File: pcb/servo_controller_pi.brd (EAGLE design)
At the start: 71 parts, among them IC1 PIC18F452, IC3 MAX4173FESA+, IC4 LM2936MP-3.3, IC5 4512D, IC6 LM386M-1, Q1 10Mhz, Q4 BC848ALT1SMD

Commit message: BleuettePi
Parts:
- removed LED2: (no value), led:CHIPLED_0805
- removed SJ1: (no value), jumper:SJ
- removed U$1: (no value), ohw-logo:OSHW_8X100_NOTEXT
- added C8: (no value), rcl:PANASONIC_A
- added HP+, HP-: (no value), wirepad:2,54/0,8
- added PWR: (no value), led:CHIPLED_0805
- added U$5: (no value), ohw-logo:OSHW_6X150_NOTEXT
- moved C17 12.9 mm to (78.4, 21.3)
- moved U$2 12.0 mm to (41.0, 18.4), turned to 0 degrees
- moved R15 8.98 mm to (70.5, 14.0), turned to 180 degrees
- moved C15 8.76 mm to (76.5, 14.0)
- moved R3 8.26 mm to (74.9, 21.3), turned to 180 degrees
- moved R12 7.63 mm to (25.7, 14.3)
- moved IC6 6.38 mm to (70.5, 20.3)
- moved C14 6.24 mm to (76.5, 17.8)
- moved SV4 4.49 mm to (81.3, 14.6)
- moved R2 4.24 mm to (13.7, 25.4)
- moved D3 4.14 mm to (10.2, 26.4)
- moved R9 4.13 mm to (25.4, 18.3)
- moved D6 3.82 mm to (27.9, 20.3)
- moved R1 3.62 mm to (7.30, 25.4), turned to 270 degrees
- moved R10 3.49 mm to (30.5, 18.3)
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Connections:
- new net N$9: C16.-, HP+.1
- net +3V3: now also PWR.C; no longer LED2.C
- net +5V: now also C8.+
- net N$39: now also PWR.A; no longer LED2.A
- net VSS: now also C8.-, HP-.1
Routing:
- net +5V: track 92.4 -> 245.8 mm, vias 1 -> 4
- net DI: track 0.00 -> 85.7 mm
- net SI: track 0.00 -> 77.2 mm
- net TX_PI: track 0.00 -> 49.3 mm, vias 0 -> 3
- net RX_PI: track 3.83 -> 46.7 mm, vias 0 -> 1
- net SDA: track 46.5 -> 78.0 mm
- net N$21: track 0.00 -> 10.4 mm
- net N$34: track 15.6 -> 24.7 mm
- net VSS: track 87.0 -> 93.8 mm, vias 10 -> 13
- net N$7: track 0.00 -> 6.76 mm
- net N$41: track 0.00 -> 6.01 mm
- net N$23: track 23.6 -> 17.7 mm
- net N$42: track 0.00 -> 5.93 mm
- net N$18: track 11.3 -> 16.8 mm
- net OPTION2: track 20.3 -> 14.8 mm
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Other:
- board text added: "BleuettePi"
- board text added: "Rev. 1.0.0"
- board text removed: "ON"
- board text removed: "Rev. 1.2.1"

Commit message: BleuettePi
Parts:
- added T3.3V, T5V, T6V: TPB1,27, testpad:B1,27
- added TP1: TPSQPAD1-13, testpad:P1-13
- moved U$2 2.62 mm to (41.6, 15.9)
- moved C12 1.85 mm to (66.7, 23.2), turned to 270 degrees
- moved R13 0.64 mm to (70.5, 33.0)
- renumbered SV5 to OPTION
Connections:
- net +3V3: now also T3.3V.TP
- net +5V: now also T5V.TP
- net VEE: now also T6V.TP
- net VSS: now also TP1.TP
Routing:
- net +5V: track 245.8 -> 243.8 mm
- net VEE: track 179.9 -> 181.5 mm
- net OUT: track 76.8 -> 75.5 mm
- net +3V3: track 176.1 -> 177.1 mm
- net N$37: track 5.75 -> 6.38 mm
- net SCL: track 74.8 -> 75.4 mm
- net VSS: vias 13 -> 10
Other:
- board text added: "3.3V"
- board text added: "5V"
- board text added: "6V"
- board text added: "GND"
- board text added: "HP"
- board text added: "L"
- board text added: "LED Strip"
- board text added: "R"
- board text removed: "-"
- board text removed: "Bleuette"

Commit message: BleuettePi
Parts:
- removed T3.3V, T5V, T6V: TPB1,27, testpad:B1,27
- added AN6, T_3.3V, T_5V, T_6V, T_LVOLTAGE, T_RX_PI, T_TX_PI: TPB1,27, testpad:B1,27
- added T_CURRENT: TPSQPAD1-13, testpad:P1-13
- HP+, HP-, P5V, PGND, PLIPO: device wirepad:2,54/0,8 -> wirepad:2,15/1,0
- moved U$5 60.7 mm to (26.4, 33.0)
- moved HP- 1.90 mm to (81.3, 23.2)
- moved P5V 1.27 mm to (3.81, 25.4)
- moved TP1 1.27 mm to (2.38, 35.9)
- moved D2 1.27 mm to (3.81, 2.54)
- moved PGND 1.27 mm to (3.81, 20.3)
- moved C16 0.32 mm to (76.2, 25.7)
- moved HP+ 0.32 mm to (81.3, 25.7)
- moved C5 0.32 mm to (2.86, 10.8)
- renumbered U$4 to IC7
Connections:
- new net N$20: IC1.27
- new net N$26: AN6.TP, IC1.26
- net +3V3: now also T_3.3V.TP; no longer T3.3V.TP
- net +5V: now also T_5V.TP; no longer T5V.TP
- net LIPO_VOLTAGE: now also T_LVOLTAGE.TP
- net RX_PI: now also T_RX_PI.TP
- net SERVO_CURRENT: now also T_CURRENT.TP
- net TX_PI: now also T_TX_PI.TP
- net VEE: now also T_6V.TP; no longer T6V.TP
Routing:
- net VSS: track 93.8 -> 107.7 mm, vias 10 -> 12
- net +5V: track 243.8 -> 241.5 mm
- net LIPO_VOLTAGE: track 46.8 -> 48.9 mm
- net N$26: track 0.00 -> 1.66 mm
- net +3V3: track 177.1 -> 175.5 mm
- net TX_PI: track 49.3 -> 50.3 mm
- net RX_PI: track 46.7 -> 47.7 mm
- net VEE: track 181.5 -> 182.3 mm
- net VDD: track 31.5 -> 32.0 mm
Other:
- board text added: "C"
- board text added: "GY-27"
- board text added: "LED STRIP"
- board text added: "RX Pi"
- board text added: "TX Pi"
- board text added: "V"
- board text removed: "LED Strip"

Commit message: RaspberryPi
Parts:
- added DRDY: (no value), jumper:SJ
- U$3: value RASPBERRY-PI -> RASPBERRY-PILIGHT-HOLE; device RaspberryPi:RASPBERRY-PI -> RaspberryPi:RASPBERRY-PI-LIGHT-HOLE
- moved U$5 60.8 mm to (79.7, 3.81)
- moved U$3 45.5 mm to (41.9, 27.9)
- moved D6 14.5 mm to (25.4, 34.6), turned to 90 degrees
- moved R9 5.91 mm to (30.5, 21.3), turned to 270 degrees
- moved SV1 3.81 mm to (73.0, 48.9)
- moved SV2 3.81 mm to (52.1, 48.9)
- moved RN1 3.18 mm to (63.5, 43.5)
- moved IC5 2.54 mm to (63.5, 36.2)
- moved C6 2.22 mm to (67.6, 30.5)
- moved R13 2.22 mm to (70.5, 35.2)
- moved C8 1.59 mm to (77.5, 32.4)
- moved R12 1.42 mm to (25.1, 13.0)
- moved T_3.3V 1.14 mm to (73.3, 30.5)
- moved R10 0.95 mm to (31.4, 18.3)
- moved R11 0.95 mm to (31.4, 16.2)
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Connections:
- new net N$36: DRDY.2, IC7.DRY
- net OPTION4: now also DRDY.1
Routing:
- net OPTION4: track 19.7 -> 66.0 mm
- net +5V: track 241.5 -> 252.8 mm, vias 4 -> 3
- net VSS: track 107.7 -> 98.8 mm, vias 12 -> 11
- net ADDRA: track 53.2 -> 49.8 mm
- net OUT: track 75.5 -> 72.4 mm
- net ADDRB: track 49.0 -> 45.9 mm
- net ADDRC: track 48.3 -> 45.2 mm
- net N$33: track 20.8 -> 23.5 mm
- net N$18: track 16.8 -> 19.5 mm
- net N$34: track 24.7 -> 27.4 mm
- net N$36: track 0.00 -> 2.59 mm
- net +3V3: track 175.5 -> 178.0 mm
- net N$28: track 13.9 -> 15.8 mm
- net RX_PI: track 47.7 -> 49.6 mm
- net N$30: track 12.8 -> 14.7 mm
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
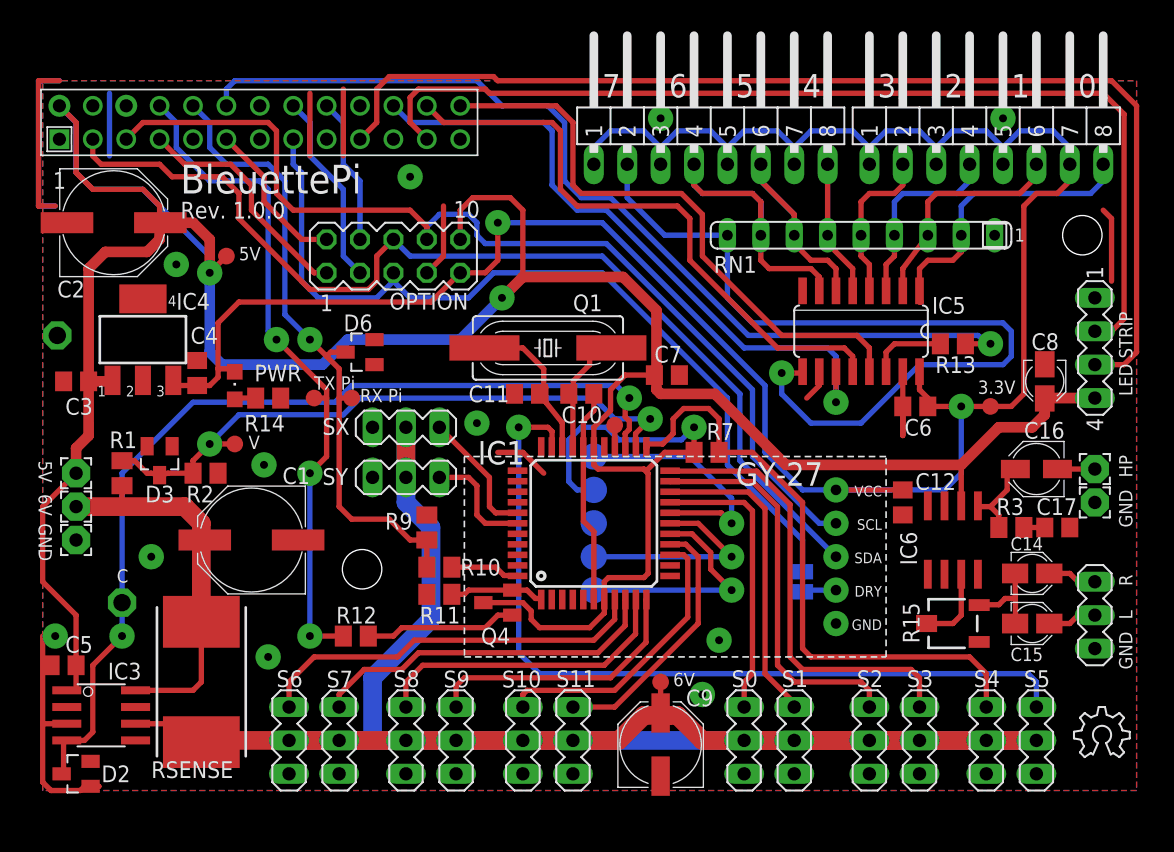
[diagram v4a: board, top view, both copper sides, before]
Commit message: Raspberry Pi PCB version
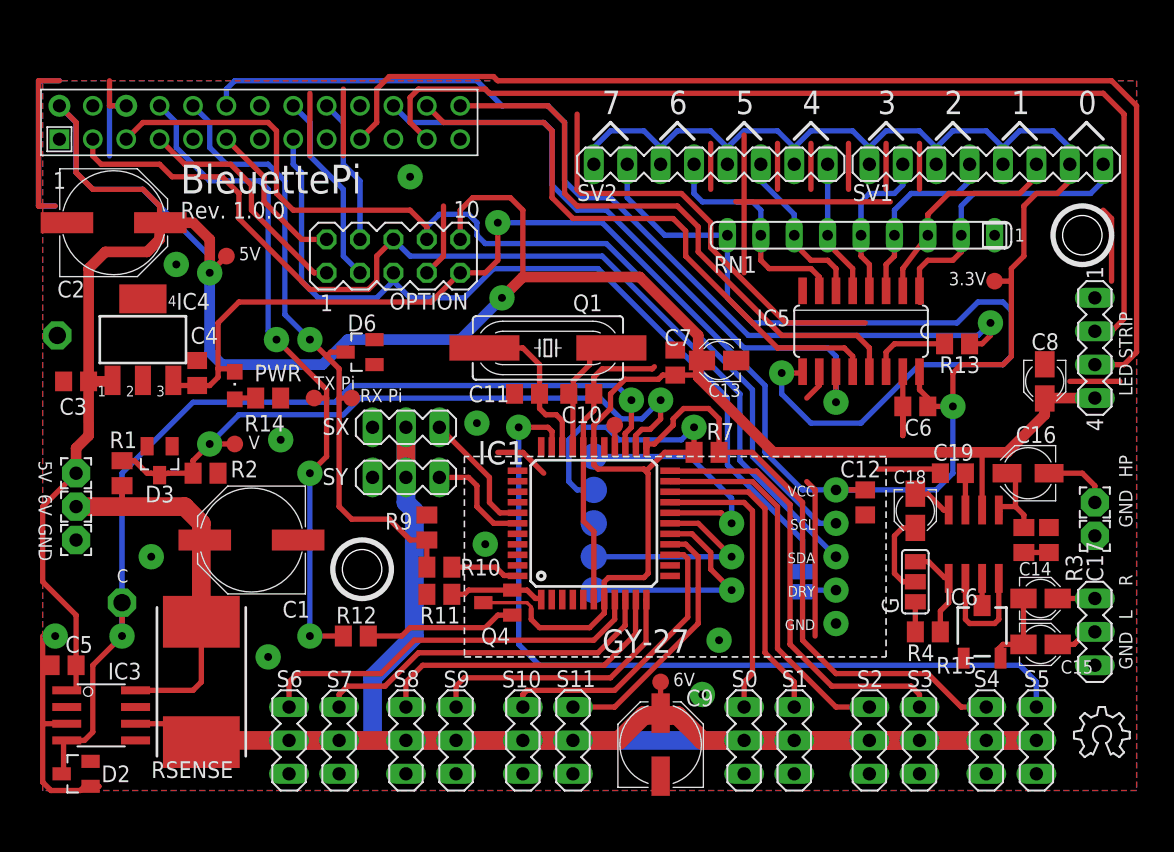
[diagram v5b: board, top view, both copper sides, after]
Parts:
- added C13: (no value), rcl:PANASONIC_A
- added C18: 10uf, rcl:PANASONIC_A
- added C19: (no value), rcl:C0805
- added G: (no value), jumper:SJ_2
- added R4: 1k, rcl:M0805
- C14, C15: value (none) -> 4.7uf
- SV1, SV2: device con-lstb:MA08-1W -> con-lstb:MA08-1
- moved T_3.3V 9.53 mm to (73.7, 40.0)
- moved C12 2.86 mm to (63.8, 23.2)
- moved HP+ 2.54 mm to (81.3, 23.2)
- moved HP- 2.54 mm to (81.3, 20.6)
- moved R15 2.31 mm to (72.7, 13.3), turned to 90 degrees
- moved C14 2.01 mm to (77.2, 15.9)
- moved C15 1.71 mm to (77.2, 12.4)
- moved IC6 1.62 mm to (72.1, 20.0)
- moved R3 1.35 mm to (75.9, 20.3), turned to 90 degrees
- moved SV4 1.27 mm to (81.3, 13.3)
- moved C17 1.14 mm to (77.8, 20.3), turned to 90 degrees
- moved C7 1.14 mm to (49.4, 33.8), turned to 90 degrees
- moved C16 0.71 mm to (76.2, 25.4)
- moved R13 0.32 mm to (70.8, 35.2)
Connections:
- new net N$38: G.3, IC6.1, R4.2
- new net N$44: G.1, R4.1
- new net N$45: C18.+, G.2
- new net N$46: C18.-, IC6.8
- new net N$47: C19.1, IC6.7
- net +5V: now also C13.+
- net VSS: now also C13.-, C19.2
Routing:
- net VSS: track 98.8 -> 215.5 mm, vias 11 -> 10
- net N$34: track 27.4 -> 17.7 mm
- net N$38: track 0.00 -> 7.40 mm
- net N$45: track 0.00 -> 6.55 mm
- net N$18: track 19.5 -> 13.1 mm
- net N$28: track 15.8 -> 10.4 mm
- net +5V: track 252.8 -> 257.8 mm
- net N$41: track 6.01 -> 2.07 mm
- net LIPO_VOLTAGE: track 48.9 -> 52.4 mm
- net N$46: track 0.00 -> 3.05 mm
- net +3V3: track 178.0 -> 175.0 mm
- net N$47: track 0.00 -> 2.80 mm
- net SERVO_CURRENT: track 71.4 -> 73.9 mm
- net N$9: track 2.84 -> 5.14 mm
- net N$44: track 0.00 -> 2.29 mm
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
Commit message: Raspberry Pi
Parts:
- added AN7, RC1, RC2, RC3, RC4, RC5, RD2, RD3, RD4, RD5, RD6, RD7: TPSQTP06SQ, testpad:TP06SQ
- added P6V: (no value), wirepad:2,15/1,0
- AN6: value TPB1,27 -> TPSQTP06SQ; device testpad:B1,27 -> testpad:TP06SQ
- moved R1 2.56 mm to (6.99, 22.9), turned to 180 degrees
- moved PGND 2.54 mm to (3.81, 17.8)
- moved T_3.3V 2.31 mm to (75.9, 39.4)
- moved DRDY 1.27 mm to (59.1, 18.4)
- moved D3 0.63 mm to (10.2, 25.7)
- moved C4 0.48 mm to (13.5, 33.0)
- moved AN6 0.32 mm to (44.8, 28.7)
- moved C18 0.32 mm to (67.6, 22.2)
- renumbered PLIPO to PBATT
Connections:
- new net +7V: C1.+, IC3.8, P6V.1, RSENSE.1
- new net N$48: IC1.5, RD7.TP
- new net N$49: IC1.4, RD6.TP
- new net N$50: IC1.3, RD5.TP
- new net N$51: IC1.2, RD4.TP
- new net N$52: IC1.36, RC2.TP
- new net N$53: IC1.35, RC1.TP
- new net N$54: IC1.37, RC3.TP
- new net N$55: IC1.42, RC4.TP
- new net N$56: IC1.43, RC5.TP
- new net N$57: IC1.41, RD3.TP
- new net N$58: IC1.40, RD2.TP
- net N$20: now also AN7.TP
- net VDD: no longer C1.+, IC3.8, RSENSE.1
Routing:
- net VDD: track 32.0 -> 2.23 mm
- net +7V: track 0.00 -> 27.6 mm
- net VSS: track 215.5 -> 224.3 mm
- net N$51: track 0.00 -> 1.37 mm
- net N$56: track 0.00 -> 1.37 mm
- net N$53: track 0.00 -> 1.37 mm
- net N$55: track 0.00 -> 1.36 mm
- net N$52: track 0.00 -> 1.36 mm
- net N$50: track 0.00 -> 1.36 mm
- net N$57: track 0.00 -> 1.36 mm
- net N$54: track 0.00 -> 1.36 mm
- net N$49: track 0.00 -> 1.36 mm
- net N$58: track 0.00 -> 1.35 mm
- net N$48: track 0.00 -> 1.35 mm
- net N$20: track 0.00 -> 1.35 mm
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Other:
- board text added: "BT"

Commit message: BleuettePi
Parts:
- removed G: (no value), jumper:SJ_2
- removed Q4: BC848ALT1SMD, transistor-npn:SOT23
- removed R11: 1k, rcl:M0805
- removed RD2: TPSQTP06SQ, testpad:TP06SQ
- removed SV1, SV2: (no value), con-lstb:MA08-1
- added C20: (no value), rcl:PANASONIC_A
- added C21: 220uf, rcl:PANASONIC_D
- added D1: 3V3, diode:SOT23
- added JP0, JP1, JP2, JP3, JP4, JP5: (no value), pinhead:1X02
- added Q2, Q3: BC848ASMD, transistor-npn:SOT23
- added R5: 470, rcl:M0805
- added R6: 3k3, rcl:M0805
- added R8: 2k2, rcl:M0805
- added T_ECHO: TPB1,27, testpad:B1,27
- added ULTRASONIC: (no value), con-lstb:MA04-1
- C16: device rcl:PANASONIC_B -> rcl:C0805
- C17: value 100nf -> 47nf
- C18: value 10uf -> (none); device rcl:PANASONIC_A -> rcl:C0805
- C19: value (none) -> 100nf
- R3: value (none) -> 10
- moved C18 35.3 mm to (41.9, 46.4), turned to 0 degrees
- moved R4 31.8 mm to (36.8, 14.0)
- moved C16 8.86 mm to (67.6, 23.2), turned to 90 degrees
- moved R12 2.56 mm to (27.6, 12.7), turned to 0 degrees
- moved R10 0.32 mm to (31.4, 18.6)
- moved RSENSE 0.32 mm to (13.7, 9.53)
- moved C19 0.32 mm to (70.2, 25.4)
- renumbered R15 to 1K
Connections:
- removed net N$35: IC5.9, RN1.9, SV2.2
- removed net N$38: G.3, IC6.1, R4.2
- removed net N$45: C18.+, G.2
- removed net N$46: C18.-, IC6.8
- removed net N$58: IC1.40, RD2.TP
- removed net OPTION4: DRDY.1, OPTION.5, U$3.15
- new net ECHO: D1.3, R6.2, R8.1, T_ECHO.TP, U$3.18
- new net INT0: IC1.40, IC5.7
- new net INT1: IC5.9, OPTION.5
- new net RX_PIC: IC1.1, Q3.3, R4.1
- new net TRIGGER: U$3.15, ULTRASONIC.3
- net +3V3: now also JP0.1, JP1.1, JP2.1, JP3.1, JP4.1, JP5.1; no longer SV1.1, SV1.3, SV1.5, SV1.7, SV2.1, SV2.3, SV2.5, SV2.7
- net +5V: now also C16.1, C18.1, C20.+, R12.2, R4.2, U$3.4, ULTRASONIC.4; no longer Q4.3
- net N$15: now also R8.2, ULTRASONIC.2; no longer IC1.1, Q4.2, R11.1
- net N$18: now also JP5.2; no longer SV2.6
- net N$21: now also Q2.3, Q3.1; no longer Q4.1
- net N$28: now also JP4.2; no longer SV2.8
- net N$29: now also JP3.2; no longer SV1.2
- net N$30: now also JP2.2; no longer SV1.4
- net N$31: now also JP1.2; no longer SV1.6
- net N$33: now also JP0.2; no longer SV1.8
- net N$34: now also DRDY.1; no longer IC5.7, RN1.8, SV2.4
- net N$42: now also C21.+; no longer C16.+
- net N$44: now also Q2.1, R5.2; no longer G.1, R4.1
- net N$9: now also C21.-; no longer C16.-
- net OPTION3: now also U$3.13; no longer U$3.18
- net TX_PI: now also R5.1; no longer R12.2
- net VSS: now also C16.2, C18.2, C20.-, D1.1, Q2.2, Q3.2, R6.1, U$3.14, U$3.20, U$3.25, U$3.9, ULTRASONIC.1; no longer R11.2
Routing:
- net INT0: track 0.00 -> 117.9 mm, vias 0 -> 2
- net N$35: track 67.8 -> 0.00 mm, vias 1 -> 0
- net OPTION4: track 65.0 -> 0.00 mm
- net VSS: track 224.3 -> 182.6 mm, vias 10 -> 8
- net +5V: track 257.8 -> 238.1 mm
- net N$34: track 17.7 -> 0.00 mm
- net N$21: track 11.6 -> 0.00 mm
- net +3V3: track 174.9 -> 164.3 mm
- net N$38: track 7.40 -> 0.00 mm
- net N$15: track 7.23 -> 0.00 mm
- net N$45: track 6.23 -> 0.00 mm
- net N$46: track 3.30 -> 0.00 mm
- net INT1: track 0.00 -> 2.78 mm, vias 0 -> 1
- net N$9: track 5.14 -> 2.62 mm
- net N$44: track 2.29 -> 0.00 mm
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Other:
- board text added: "Vérifier la taille du potentiomètre son"
- board text removed: "6"
- board text removed: "7"

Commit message: BleuettePi
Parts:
- added R11, R15: 10, rcl:M0805
- moved C18 10.6 mm to (51.8, 50.2), turned to 270 degrees
- moved T_ECHO 9.47 mm to (41.9, 46.4)
- moved R12 6.42 mm to (34.0, 13.7)
- moved R5 6.36 mm to (25.4, 13.0)
- moved DRDY 6.02 mm to (64.8, 16.5), turned to 0 degrees
- moved Q2 1.59 mm to (28.9, 14.3)
- moved IC5 1.59 mm to (63.5, 37.8)
- moved D1 1.42 mm to (49.2, 46.0), turned to 90 degrees
- moved R13 1.31 mm to (70.5, 36.5)
- moved C6 1.31 mm to (67.9, 31.8), turned to 270 degrees
- moved Q3 1.31 mm to (33.0, 16.2)
- moved RN1 1.14 mm to (64.1, 44.5)
- moved R4 1.00 mm to (37.1, 14.9), turned to 270 degrees
- moved R6 0.90 mm to (45.4, 46.0)
- moved R10 0.71 mm to (30.8, 18.9)
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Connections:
- removed net N$34: DRDY.1
- net +5V: no longer U$3.4
- net INT1: now also DRDY.1
- net N$41: now also R11.1, R15.2
- net N$7: now also R11.2
- net VSS: now also R15.1; no longer U$3.14, U$3.20, U$3.25, U$3.9
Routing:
- net TRIGGER: track 0.00 -> 40.8 mm, vias 0 -> 1
- net INT1: track 2.78 -> 40.0 mm
- net ECHO: track 0.00 -> 33.2 mm, vias 0 -> 1
- net VSS: track 182.6 -> 197.3 mm, vias 8 -> 10
- net OPTION3: track 9.42 -> 23.3 mm
- net +5V: track 238.1 -> 251.1 mm
- net N$21: track 0.00 -> 9.47 mm
- net N$41: track 2.07 -> 9.74 mm
- net N$7: track 6.39 -> 13.3 mm
- net RX_PIC: track 1.37 -> 5.74 mm
- net N$33: track 23.2 -> 19.4 mm
- net ADDRB: track 45.5 -> 41.9 mm
- net ADDRA: track 49.8 -> 46.6 mm
- net LIPO_VOLTAGE: track 53.0 -> 49.9 mm
- net N$30: track 14.9 -> 11.8 mm
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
